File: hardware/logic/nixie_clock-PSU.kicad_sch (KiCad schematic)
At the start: 46 parts, among them J4 USB_C_PD, Q1 2N7002NXAKR, Q2 DMP3098LSD-13, U3 1364 HVPS, U3 CYPD3177-24LQXQ, U5 TPS62933FDRL

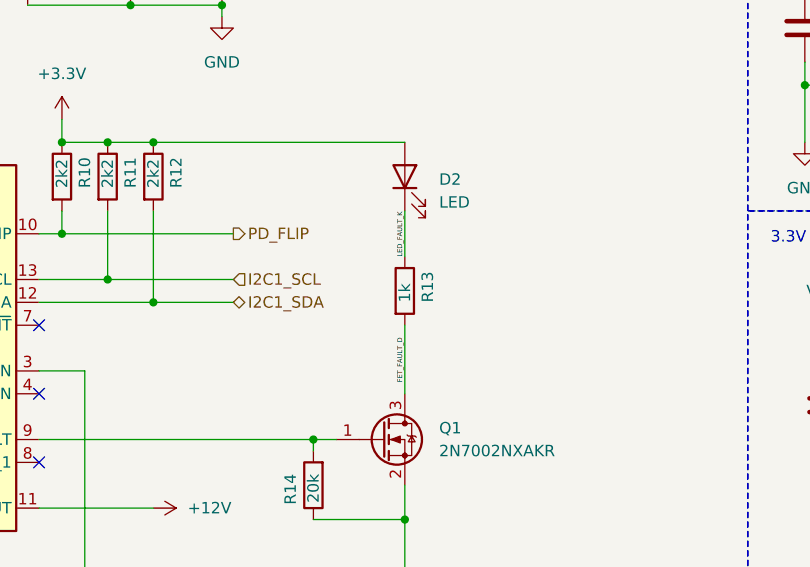
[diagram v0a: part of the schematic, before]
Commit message: Changed connectors to driver board, fixed oscillator connections
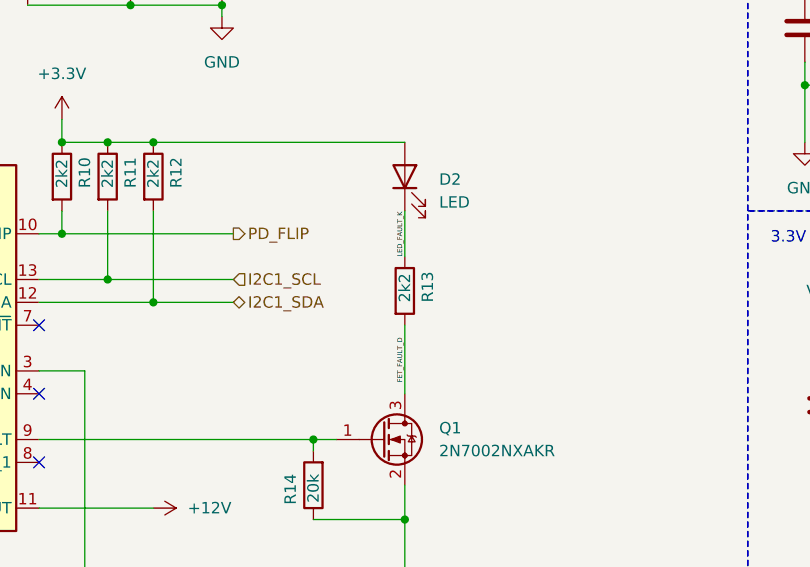
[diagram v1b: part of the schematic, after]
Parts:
- R13: value 1k -> 2k2
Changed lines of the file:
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@@
       (effects (font (size 1.27 1.27)) (justify left))
     )
-    (property "Value" "1k" (at 151.13 67.31 90)
+    (property "Value" "2k2" (at 151.13 67.31 90)
       (effects (font (size 1.27 1.27)) (justify left))
     )

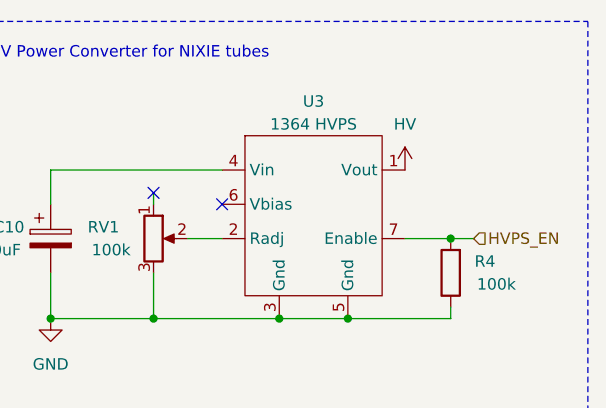
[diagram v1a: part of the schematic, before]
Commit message: Inital PCB placement
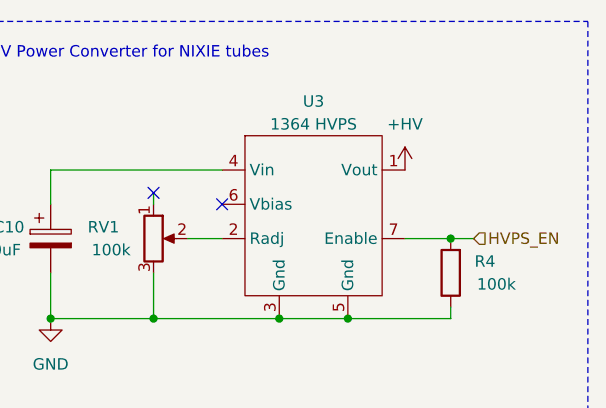
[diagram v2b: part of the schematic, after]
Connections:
- net VDD renamed +HV
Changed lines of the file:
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@@
     (effects (font (size 1.27 1.27)) (justify left))
+  )
+  (symbol (lib_id "Project:+HV") (at 264.16 29.21 0) (unit 1)
+    (in_bom yes) (on_board yes) (dnp no) (fields_autoplaced)
+    (property "Reference" "#PWR037" (at 264.16 33.02 0)
+      (effects (font (size 1.27 1.27)) hide)
+    )
+    (property "Value" "+HV" (at 264.16 24.13 0)
+      (effects (font (size 1.27 1.27)))
+    )
+    (property "Footprint" "" (at 264.16 29.21 0)
+      (effects (font (size 1.27 1.27)) hide)
+    )
+    (property "Datasheet" "" (at 264.16 29.21 0)
+      (effects (font (size 1.27 1.27)) hide)
+    )
+    (pin "1")
+    (instances
+      (project "nixie_clock"
+        (path "/7cd62b6d-1f0b-4e43-a8ba-fed6cb13f0ee/398b7551-f2fb-4418-b429-2e2b9b5009f5"
+          (reference "#PWR037") (unit 1)
+        )
+      )
+    )
   )
   (symbol (lib_id "Interface_USB:CYPD3177-24LQ") (at 92.71 72.39 0) (unit 1)
@@
         )
       )
-    )
-  )
-  (symbol (lib_id "NIXIE:HV") (at 264.16 29.21 0) (unit 1)
-    (in_bom yes) (on_board yes) (dnp no) (fields_autoplaced)
-    (property "Reference" "#PWR053" (at 264.16 33.02 0)
-      (effects (font (size 1.27 1.27)) hide)
-    )
-    (property "Value" "HV" (at 264.16 24.13 0)
-      (effects (font (size 1.27 1.27)))
-    )
-    (property "Footprint" "" (at 264.16 29.21 0)
-      (effects (font (size 1.27 1.27)) hide)
-    )
-    (property "Datasheet" "" (at 264.16 29.21 0)
-      (effects (font (size 1.27 1.27)) hide)
-    )
-    (pin "1")
-    (instances
-      (project "nixie_clock"
-        (path "/7cd62b6d-1f0b-4e43-a8ba-fed6cb13f0ee/bd582945-be48-488e-b6a0-381dd739aa42"
-          (reference "#PWR053") (unit 1)
-        )
-        (path "/7cd62b6d-1f0b-4e43-a8ba-fed6cb13f0ee/398b7551-f2fb-4418-b429-2e2b9b5009f5"
-          (reference "#PWR026") (unit 1)
-        )
-      )
